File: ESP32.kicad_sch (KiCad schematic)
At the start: 20 parts, among them Q1 SS8050-G, Q2 SS8050-G, U7 DF52-8S-0.8H(21), U8 ESP32-WROOM-32E-H4, U9 CP2102N-A02-GQFN24R

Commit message: routed, gotta check da pinz
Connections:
- net MOSI: now also U8.33 (IO21); no longer U8.37 (IO23)
- no-connect marks 17 -> 18
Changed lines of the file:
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@@
   (no_connect (at 257.175 126.365))
   (no_connect (at 211.455 136.525))
+  (no_connect (at 85.09 118.11))
   (no_connect (at 211.455 128.905))
   (no_connect (at 257.175 139.065))
@@
     (stroke (width 0) (type default))
   )
+  (wire (pts (xy 89.535 111.76) (xy 85.09 111.76))
+    (stroke (width 0) (type default))
+  )
   (wire (pts (xy 231.775 82.55) (xy 229.87 82.55))
     (stroke (width 0) (type default))
@@
     (stroke (width 0) (type default))
   )
+  (wire (pts (xy 29.21 38.735) (xy 29.21 40.005))
+    (stroke (width 0) (type default))
+  )
+  (wire (pts (xy 264.795 108.585) (xy 264.795 106.045))
+    (stroke (width 0) (type default))
+  )
+  (wire (pts (xy 69.85 33.02) (xy 76.2 33.02))
+    (stroke (width 0) (type default))
+  )
   (wire (pts (xy 90.805 106.68) (xy 85.09 106.68))
     (stroke (width 0) (type default))
   )
-  (wire (pts (xy 29.21 38.735) (xy 29.21 40.005))
-    (stroke (width 0) (type default))
-  )
-  (wire (pts (xy 264.795 108.585) (xy 264.795 106.045))
-    (stroke (width 0) (type default))
-  )
-  (wire (pts (xy 69.85 33.02) (xy 76.2 33.02))
-    (stroke (width 0) (type default))
-  )
   (wire (pts (xy 220.345 80.01) (xy 220.345 69.215))
     (stroke (width 0) (type default))
@@
   )
   (wire (pts (xy 85.09 91.44) (xy 97.155 91.44))
-    (stroke (width 0) (type default))
-  )
-  (wire (pts (xy 89.535 118.11) (xy 85.09 118.11))
     (stroke (width 0) (type default))
   )
@@
     (effects (font (size 1.27 1.27)) (justify left bottom))
   )
+  (label "ESP32_SCK" (at 90.805 106.68 0) (fields_autoplaced)
+    (effects (font (size 1.27 1.27)) (justify left bottom))
+  )
   (label "3V3" (at 97.79 31.75 180) (fields_autoplaced)
     (effects (font (size 1.27 1.27)) (justify right bottom))
   )
-  (label "ESP32_MOSI" (at 89.535 118.11 0) (fields_autoplaced)
+  (label "ESP32_MOSI" (at 89.535 111.76 0) (fields_autoplaced)
     (effects (font (size 1.27 1.27)) (justify left bottom))
   )
@@
     (effects (font (size 1.27 1.27)) (justify right bottom))
   )
-  (label "ESP32_SCK" (at 90.805 106.68 0) (fields_autoplaced)
-    (effects (font (size 1.27 1.27)) (justify left bottom))
-  )
   (label "EN" (at 241.3 63.5 0) (fields_autoplaced)

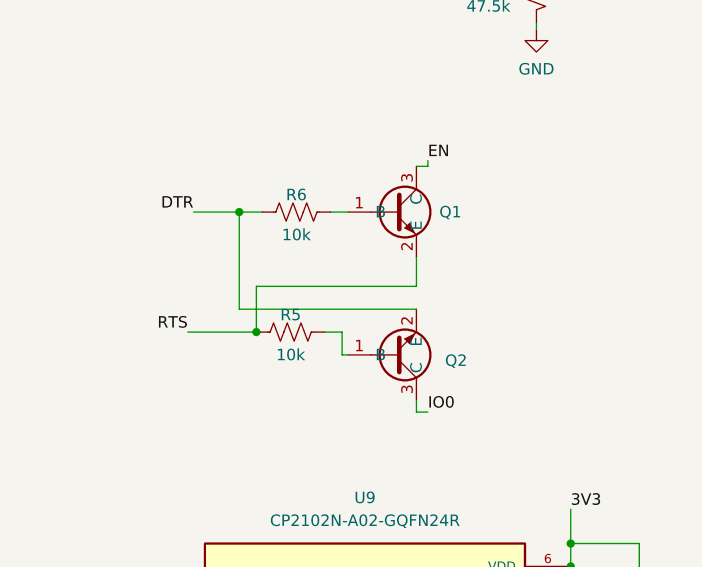
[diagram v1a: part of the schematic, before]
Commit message: bom fix for fets, now refers to the part i am actually using not the one which doesn't work right. Library changes for parts missing courtyards, drc passing
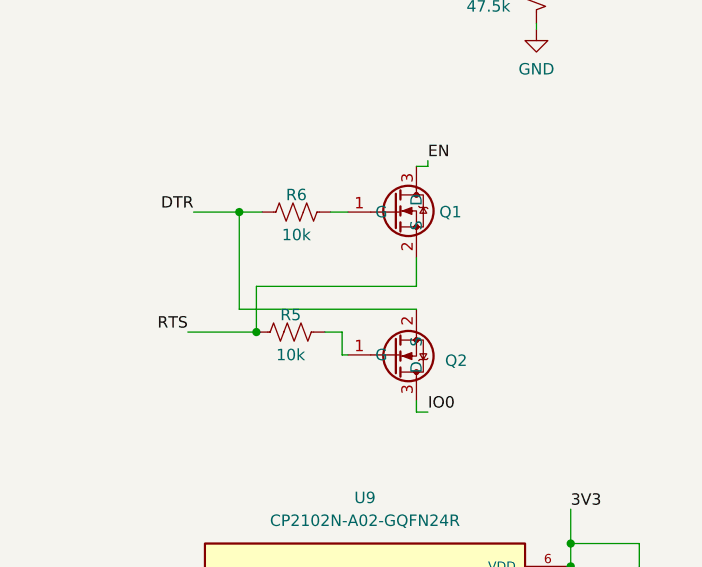
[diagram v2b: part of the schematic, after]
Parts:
- Q1: value SS8050-G -> SSM3K15F,LF; symbol robot-cortex:SS8050-G -> robot-cortex:SSM3K15F,LF
- Q2: symbol robot-cortex:SS8050-G -> robot-cortex:SSM3K15F,LF
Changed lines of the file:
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@@
     )
   )
-  (symbol (lib_id "robot-cortex:SS8050-G") (at 232.41 85.09 0) (mirror x) (unit 1)
+  (symbol (lib_id "robot-cortex:SSM3K15F,LF") (at 232.41 85.09 0) (mirror x) (unit 1)
     (in_bom yes) (on_board yes) (dnp no)
     (property "Reference" "Q2" (at 243.205 85.725 0)
@@
       (effects (font (size 1.27 1.27)) hide)
     )
-    (property "Datasheet" "" (at 232.41 85.09 0)
+    (property "Datasheet" "https://toshiba.semicon-storage.com/info/docget.jsp?did=22719&prodName=SSM3K15F" (at 232.41 85.09 0)
       (effects (font (size 1.27 1.27)) hide)
     )
@@
     )
   )
-  (symbol (lib_id "robot-cortex:SS8050-G") (at 232.41 69.215 0) (unit 1)
+  (symbol (lib_id "robot-cortex:SSM3K15F,LF") (at 232.41 69.215 0) (unit 1)
     (in_bom yes) (on_board yes) (dnp no) (fields_autoplaced)
     (property "Reference" "Q1" (at 242.57 69.215 0)
       (effects (font (size 1.27 1.27)) (justify left))
     )
-    (property "Value" "SS8050-G" (at 227.33 61.595 0)
+    (property "Value" "SSM3K15F,LF" (at 227.33 61.595 0)
       (effects (font (size 1.27 1.27)) hide)
     )
@@
       (effects (font (size 1.27 1.27)) hide)
     )
-    (property "Datasheet" "" (at 232.41 69.215 0)
+    (property "Datasheet" "https://toshiba.semicon-storage.com/info/docget.jsp?did=22719&prodName=SSM3K15F" (at 232.41 69.215 0)
       (effects (font (size 1.27 1.27)) hide)
     )

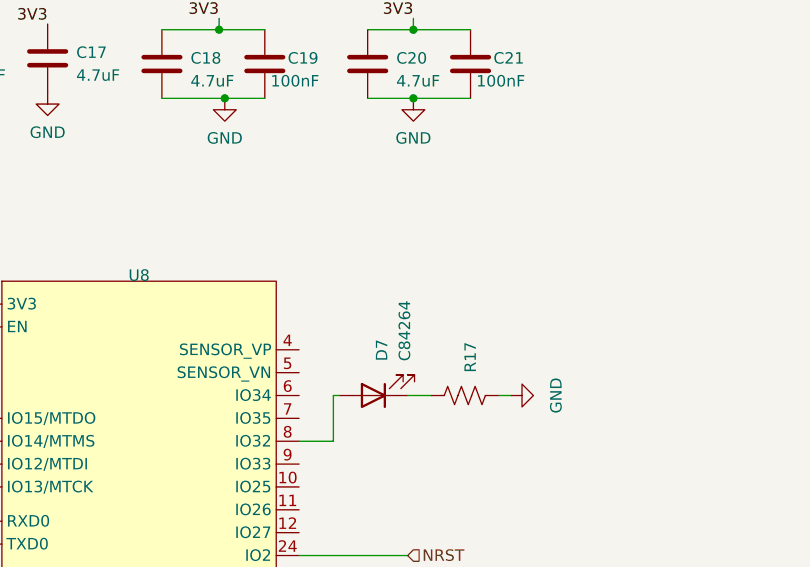
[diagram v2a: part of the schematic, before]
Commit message: bom cleanup - caps not hardcoded lcsc part, led replaced
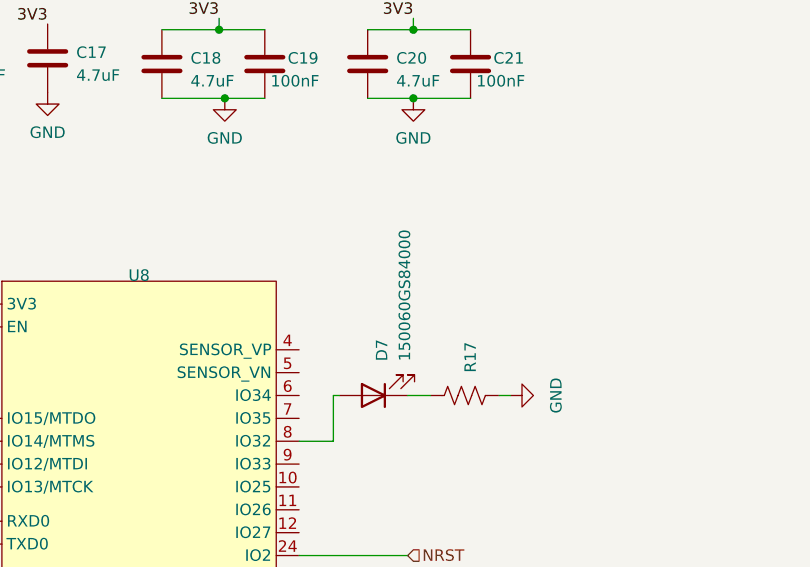
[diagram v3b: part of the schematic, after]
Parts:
- D7: value C84264 -> 150060GS84000
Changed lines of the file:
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@@
       (effects (font (size 1.27 1.27)) (justify right))
     )
-    (property "Value" "C84264" (at 96.8375 69.85 90)
+    (property "Value" "150060GS84000" (at 96.8375 69.85 90)
       (effects (font (size 1.27 1.27)) (justify right))
     )
@@
       (effects (font (size 1.27 1.27)) hide)
     )
-    (property "Datasheet" "~" (at 93.345 73.66 0)
+    (property "Datasheet" "https://www.we-online.com/components/products/datasheet/150060GS84000.pdf" (at 93.345 73.66 0)
       (effects (font (size 1.27 1.27)) hide)
     )

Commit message: more bom
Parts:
- Q2: value SS8050-G -> SSM3K15F,LF
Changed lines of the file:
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@@
       (effects (font (size 1.27 1.27)) (justify left))
     )
-    (property "Value" "SS8050-G" (at 227.33 92.71 0)
+    (property "Value" "SSM3K15F,LF" (at 227.33 92.71 0)
       (effects (font (size 1.27 1.27)) hide)
     )
